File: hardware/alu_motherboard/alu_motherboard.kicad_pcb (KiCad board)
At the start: 4 copper layers, 40 x 284 mm, 113 parts, among them J1 ADD_SUB, J2 Conn_02x26_Odd_Even, J3 BITOPS, J4 SHIFT, Q1 IRLML6244, Q10 IRLML6244, Q11 IRLML6244, Q12 IRLML6244, Q13 IRLML6244, Q14 IRLML6244, Q15 IRLML6244, Q16 IRLML6244, Q2 IRLML6244, Q3 IRLML6244, Q4 IRLML6244, Q5 IRLML6244, Q6 IRLML6244, Q7 IRLML6244, Q8 IRLML6244, Q9 IRLML6244, U1 74HC00, U10 74HC00, U11 74HC00, U12 74HC00, U13 74HC00, U14 74HC00, U15 74HC00, U16 74HC00, U17 74HC00, U18 74HC00, U19 74HC00, U2 74HC00, U20 74HC00, U21 74HC00, U3 74HC00, U4 74HC00, U5 74HC00, U6 74HC00, U7 74HC00, U8 74HC00, U9 74HC00

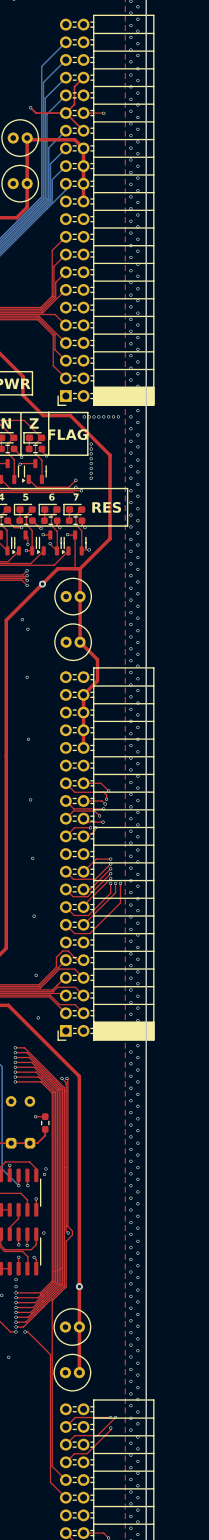
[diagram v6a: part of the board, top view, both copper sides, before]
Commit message: ALU shifter, bitops and motherboard as ordered
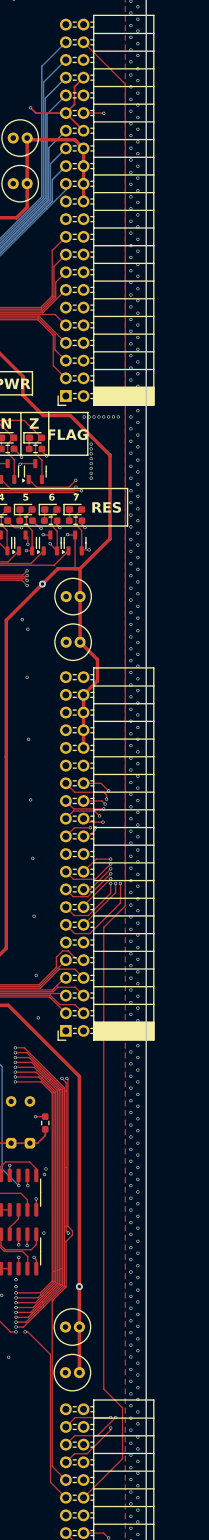
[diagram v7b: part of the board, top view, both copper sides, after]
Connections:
- J4 pad 24: +5V -> /ACIN
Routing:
- net /ACIN: track 14.2 -> 230.4 mm
- net +5V: track 803.5 -> 801.0 mm
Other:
- board text added: "SIB"
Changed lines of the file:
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@@
 		(sheetname "Root")
 		(sheetfile "alu_motherboard.kicad_sch")
-		(attr through_hole exclude_from_bom dnp)
+		(attr through_hole exclude_from_pos_files exclude_from_bom dnp)
 		(fp_rect
 			(start -4 -1.25)
@@
 		(sheetname "Root")
 		(sheetfile "alu_motherboard.kicad_sch")
-		(attr through_hole exclude_from_bom dnp)
+		(attr through_hole exclude_from_pos_files exclude_from_bom dnp)
 		(fp_circle
 			(center 1 0)
@@
 		(sheetname "Root")
 		(sheetfile "alu_motherboard.kicad_sch")
-		(attr through_hole exclude_from_bom dnp)
+		(attr through_hole exclude_from_pos_files exclude_from_bom dnp)
 		(fp_rect
 			(start -4 -1.25)
@@
 		(sheetname "Root")
 		(sheetfile "alu_motherboard.kicad_sch")
-		(attr through_hole exclude_from_bom dnp)
+		(attr through_hole exclude_from_pos_files exclude_from_bom dnp)
 		(fp_rect
 			(start -4 -1.25)
@@
 		(sheetname "Root")
 		(sheetfile "alu_motherboard.kicad_sch")
-		(attr through_hole exclude_from_bom dnp)
+		(attr through_hole exclude_from_pos_files exclude_from_bom dnp)
 		(fp_circle
 			(center 1 0)
@@
 		(sheetname "Root")
 		(sheetfile "alu_motherboard.kicad_sch")
-		(attr through_hole exclude_from_bom dnp)
+		(attr through_hole exclude_from_pos_files exclude_from_bom dnp)
 		(fp_circle
 			(center 1 0)
@@
 		(sheetname "Root")
 		(sheetfile "alu_motherboard.kicad_sch")
-		(attr through_hole exclude_from_bom dnp)
+		(attr through_hole exclude_from_pos_files exclude_from_bom dnp)
 		(fp_circle
 			(center 1 0)
@@
 		(sheetname "Root")
 		(sheetfile "alu_motherboard.kicad_sch")
-		(attr through_hole exclude_from_bom dnp)
+		(attr through_hole exclude_from_pos_files exclude_from_bom dnp)
 		(fp_circle
 			(center 1 0)
@@
 			(layers "*.Cu" "*.Mask")
 			(remove_unused_layers no)
-			(net 2 "+5V")
+			(net 115 "/ACIN")
 			(pinfunction "Pin_24")
 			(pintype "passive")
@@
 		(sheetname "Root")
 		(sheetfile "alu_motherboard.kicad_sch")
-		(attr through_hole exclude_from_bom dnp)
+		(attr through_hole exclude_from_pos_files exclude_from_bom dnp)
 		(fp_circle
 			(center 1 0)
@@
 		(sheetname "Root")
 		(sheetfile "alu_motherboard.kicad_sch")
-		(attr through_hole exclude_from_bom dnp)
+		(attr through_hole exclude_from_pos_files exclude_from_bom dnp)
 		(fp_rect
 			(start -4 -1.25)
@@
 		(sheetname "Root")
 		(sheetfile "alu_motherboard.kicad_sch")
-		(attr through_hole exclude_from_bom dnp)
+		(attr through_hole exclude_from_pos_files exclude_from_bom dnp)
 		(fp_rect
 			(start -4 -1.25)
@@
 		)
 	)
-	(gr_text "VCC"
+	(gr_text "SIB"
 		(at 194.7 285.3 0)
 		(layer "B.SilkS")
@@
 	)
 	(segment
+		(start 200.8 275.25)
+		(end 200.8 282.87)
+		(width 0.5)
+		(layer "In2.Cu")
+		(net 2)
+	)
+	(segment
 		(start 200.2 267.45)
 		(end 202.6 269.85)
@@
 	)
 	(segment
-		(start 200.8 275.25)
-		(end 200.8 285.41)
-		(width 0.5)
-		(layer "In2.Cu")
-		(net 2)
-	)
-	(segment
 		(start 174.9 240.9)
 		(end 186 240.9)
@@
 	)
 	(segment
+		(start 206.8 200.4)
+		(end 203.7 203.5)
+		(width 0.15)
+		(layer "F.Cu")
+		(net 115)
+	)
+	(segment
+		(start 206.4 279.81)
+		(end 200.8 285.41)
+		(width 0.15)
+		(layer "F.Cu")
+		(net 115)
+	)
+	(segment
+		(start 200.8 76.4)
+		(end 206.8 82.4)
+		(width 0.15)
+		(layer "F.Cu")
+		(net 115)
+	)
+	(segment
 		(start 190.81 68.55)
 		(end 190.81 70.19)
@@
 	)
 	(segment
+		(start 206.8 82.4)
+		(end 206.8 200.4)
+		(width 0.15)
+		(layer "F.Cu")
+		(net 115)
+	)
+	(segment
 		(start 190.81 70.19)
 		(end 190.8 70.2)
 		(width 0.15)
 		(layer "F.Cu")
+		(net 115)
+	)
+	(segment
+		(start 206.4 272.5)
+		(end 206.4 279.81)
+		(width 0.15)
+		(layer "F.Cu")
+		(net 115)
+	)
+	(segment
+		(start 203.7 269.8)
+		(end 206.4 272.5)
+		(width 0.15)
+		(layer "F.Cu")
+		(net 115)
+	)
+	(segment
+		(start 203.7 203.5)
+		(end 203.7 269.8)
+		(width 0.15)
+		(layer "F.Cu")
